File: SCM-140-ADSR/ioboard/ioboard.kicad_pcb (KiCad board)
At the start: 2 copper layers, 108 x 48.3 mm, 25 parts

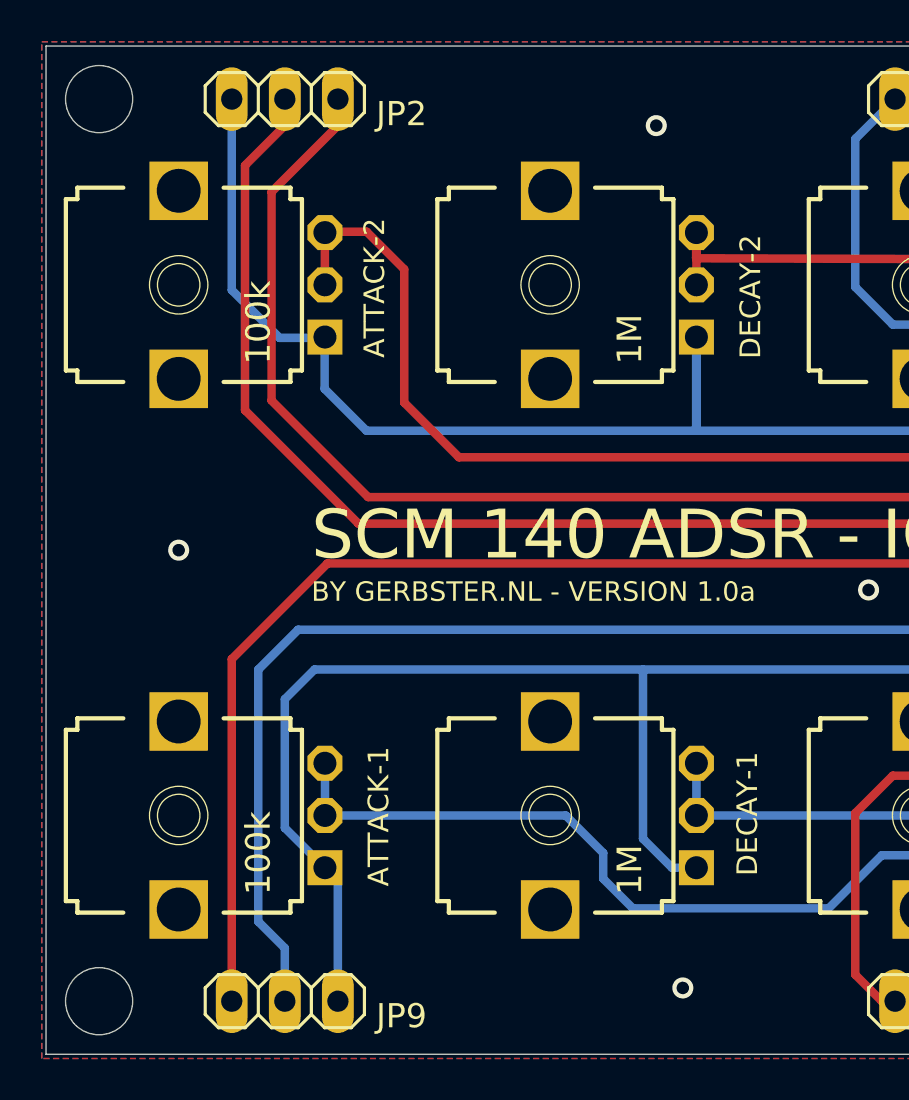
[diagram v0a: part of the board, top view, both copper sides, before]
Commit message: Add M3 mounting holes for mechanical stability
In case non-threaded potentiometers are used
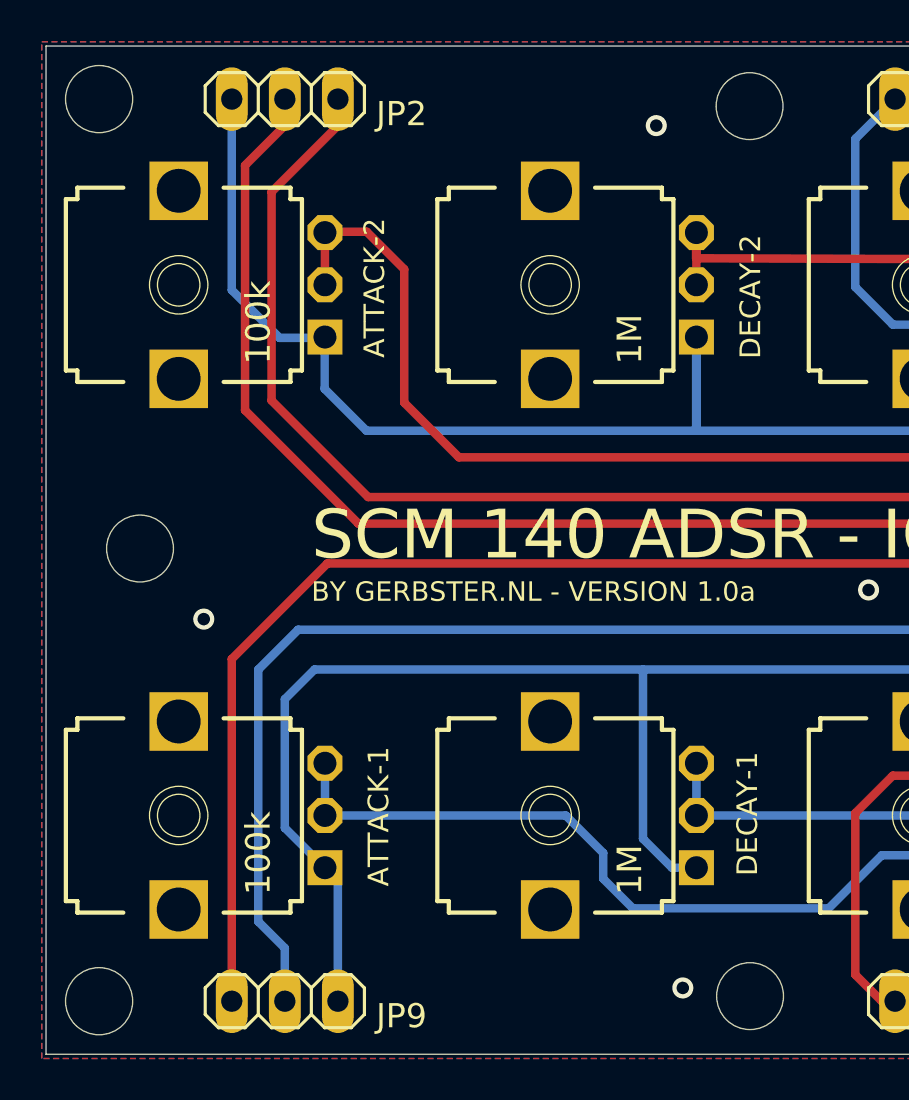
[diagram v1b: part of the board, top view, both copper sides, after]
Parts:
- added REF**: MountingHole_3.2mm_M3, MountingHole:MountingHole_3.2mm_M3, F.Cu at (128.2, 83.8)
- added REF**: MountingHole_3.2mm_M3, MountingHole:MountingHole_3.2mm_M3, F.Cu at (99.0, 104.9)
- added REF**: MountingHole_3.2mm_M3, MountingHole:MountingHole_3.2mm_M3, F.Cu at (128.2, 126.3)
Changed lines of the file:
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@@
       (connect_pads (clearance 0))
       (min_thickness 0.254)
-      (keepout (tracks not_allowed) (vias not_allowed) (pads not_allowed ) (copperpour not_allowed) (footprints not_allowed))
+      (keepout (tracks not_allowed) (vias not_allowed) (pads not_allowed) (copperpour not_allowed) (footprints not_allowed))
       (fill (thermal_gap 0.508) (thermal_bridge_width 0.508))
       (polygon
@@
       (net 20 "GATE-2") (solder_mask_margin 0.1016))
   )
+  (footprint "MountingHole:MountingHole_3.2mm_M3" (layer "F.Cu")
+    (at 128.201278 83.75 90)
+    (descr "Mounting Hole 3.2mm, no annular, M3")
+    (tags "mounting hole 3.2mm no annular m3")
+    (attr exclude_from_pos_files exclude_from_bom)
+    (fp_text reference "REF**" (at 0 -4.2 90) (layer "F.SilkS") hide
+      (effects (font (size 1 1) (thickness 0.15)))
+    )
+    (fp_text value "MountingHole_3.2mm_M3" (at 0 4.2 90) (layer "F.Fab")
+      (effects (font (size 1 1) (thickness 0.15)))
+    )
+    (fp_text user "${REFERENCE}" (at 0 0 90) (layer "F.Fab")
+      (effects (font (size 1 1) (thickness 0.15)))
+    )
+    (fp_circle (center 0 0) (end 3.2 0) (layer "Cmts.User") (width 0.15) (fill none))
+    (fp_circle (center 0 0) (end 3.45 0) (layer "F.CrtYd") (width 0.05) (fill none))
+    (pad "" np_thru_hole circle (at 0 0 90) (size 3.2 3.2) (drill 3.2) (layers *.Cu *.Mask))
+  )
   (footprint "" (layer "F.Cu")
     (at 199.9361 83.4136)
@@
       (connect_pads (clearance 0))
       (min_thickness 0.254)
-      (keepout (tracks not_allowed) (vias not_allowed) (pads not_allowed ) (copperpour not_allowed) (footprints not_allowed))
+      (keepout (tracks not_allowed) (vias not_allowed) (pads not_allowed) (copperpour not_allowed) (footprints not_allowed))
       (fill (thermal_gap 0.508) (thermal_bridge_width 0.508))
       (polygon
@@
       (connect_pads (clearance 0))
       (min_thickness 0.254)
-      (keepout (tracks not_allowed) (vias not_allowed) (pads not_allowed ) (copperpour not_allowed) (footprints not_allowed))
+      (keepout (tracks not_allowed) (vias not_allowed) (pads not_allowed) (copperpour not_allowed) (footprints not_allowed))
       (fill (thermal_gap 0.508) (thermal_bridge_width 0.508))
       (polygon
@@
       (connect_pads (clearance 0))
       (min_thickness 0.254)
-      (keepout (tracks not_allowed) (vias not_allowed) (pads not_allowed ) (copperpour not_allowed) (footprints not_allowed))
+      (keepout (tracks not_allowed) (vias not_allowed) (pads not_allowed) (copperpour not_allowed) (footprints not_allowed))
       (fill (thermal_gap 0.508) (thermal_bridge_width 0.508))
       (polygon
@@
     )
   )
+  (footprint "MountingHole:MountingHole_3.2mm_M3" (layer "F.Cu")
+    (at 99.025 104.925 90)
+    (descr "Mounting Hole 3.2mm, no annular, M3")
+    (tags "mounting hole 3.2mm no annular m3")
+    (attr exclude_from_pos_files exclude_from_bom)
+    (fp_text reference "REF**" (at 0 -4.2 90) (layer "F.SilkS") hide
+      (effects (font (size 1 1) (thickness 0.15)))
+    )
+    (fp_text value "MountingHole_3.2mm_M3" (at 0 4.2 90) (layer "F.Fab")
+      (effects (font (size 1 1) (thickness 0.15)))
+    )
+    (fp_text user "${REFERENCE}" (at 0 0 90) (layer "F.Fab")
+      (effects (font (size 1 1) (thickness 0.15)))
+    )
+    (fp_circle (center 0 0) (end 3.2 0) (layer "Cmts.User") (width 0.15) (fill none))
+    (fp_circle (center 0 0) (end 3.45 0) (layer "F.CrtYd") (width 0.05) (fill none))
+    (pad "" np_thru_hole circle (at 0 0 90) (size 3.2 3.2) (drill 3.2) (layers *.Cu *.Mask))
+  )
   (footprint "ioboard:EVUF" (layer "F.Cu")
     (at 136.4361 92.3036 90)
@@
       (connect_pads (clearance 0))
       (min_thickness 0.254)
-      (keepout (tracks not_allowed) (vias not_allowed) (pads not_allowed ) (copperpour not_allowed) (footprints not_allowed))
+      (keepout (tracks not_allowed) (vias not_allowed) (pads not_allowed) (copperpour not_allowed) (footprints not_allowed))
       (fill (thermal_gap 0.508) (thermal_bridge_width 0.508))
       (polygon
@@
     )
   )
+  (footprint "MountingHole:MountingHole_3.2mm_M3" (layer "F.Cu")
+    (at 128.225 126.35 90)
+    (descr "Mounting Hole 3.2mm, no annular, M3")
+    (tags "mounting hole 3.2mm no annular m3")
+    (attr exclude_from_pos_files exclude_from_bom)
+    (fp_text reference "REF**" (at 0 -4.2 90) (layer "F.SilkS") hide
+      (effects (font (size 1 1) (thickness 0.15)))
+    )
+    (fp_text value "MountingHole_3.2mm_M3" (at 0 4.2 90) (layer "F.Fab")
+      (effects (font (size 1 1) (thickness 0.15)))
+    )
+    (fp_text user "${REFERENCE}" (at 0 0 90) (layer "F.Fab")
+      (effects (font (size 1 1) (thickness 0.15)))
+    )
+    (fp_circle (center 0 0) (end 3.2 0) (layer "Cmts.User") (width 0.15) (fill none))
+    (fp_circle (center 0 0) (end 3.45 0) (layer "F.CrtYd") (width 0.05) (fill none))
+    (pad "" np_thru_hole circle (at 0 0 90) (size 3.2 3.2) (drill 3.2) (layers *.Cu *.Mask))
+  )
   (footprint "ioboard:EVUF" (layer "F.Cu")
     (at 100.8761 117.7036 90)
@@
       (connect_pads (clearance 0))
       (min_thickness 0.254)
-      (keepout (tracks not_allowed) (vias not_allowed) (pads not_allowed ) (copperpour not_allowed) (footprints not_allowed))
+      (keepout (tracks not_allowed) (vias not_allowed) (pads not_allowed) (copperpour not_allowed) (footprints not_allowed))
       (fill (thermal_gap 0.508) (thermal_bridge_width 0.508))
       (polygon
@@
   (segment (start 180.8861 103.7336) (end 184.0611 100.5586) (width 0.4064) (layer "F.Cu") (net 22))
   (segment (start 109.47654 103.7336) (end 180.8861 103.7336) (width 0.4064) (layer "F.Cu") (net 22))
-  (via (at 100.8761 105.0036) (size 1.0064) (drill 0.6) (layers "F.Cu" "B.Cu") (net 23))
+  (via (at 102.0761 108.3036) (size 1.0064) (drill 0.6) (layers "F.Cu" "B.Cu") (net 23))
   (via (at 162.4711 84.6836) (size 1.0064) (drill 0.6) (layers "F.Cu" "B.Cu") (net 23))
   (via (at 195.4911 103.0986) (size 1.0064) (drill 0.6) (layers "F.Cu" "B.Cu") (net 23))
